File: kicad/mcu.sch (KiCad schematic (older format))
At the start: 25 parts, among them J7 UEXT, U2 STM32G431CBTx, U6 24AA01, Y1 8MHz

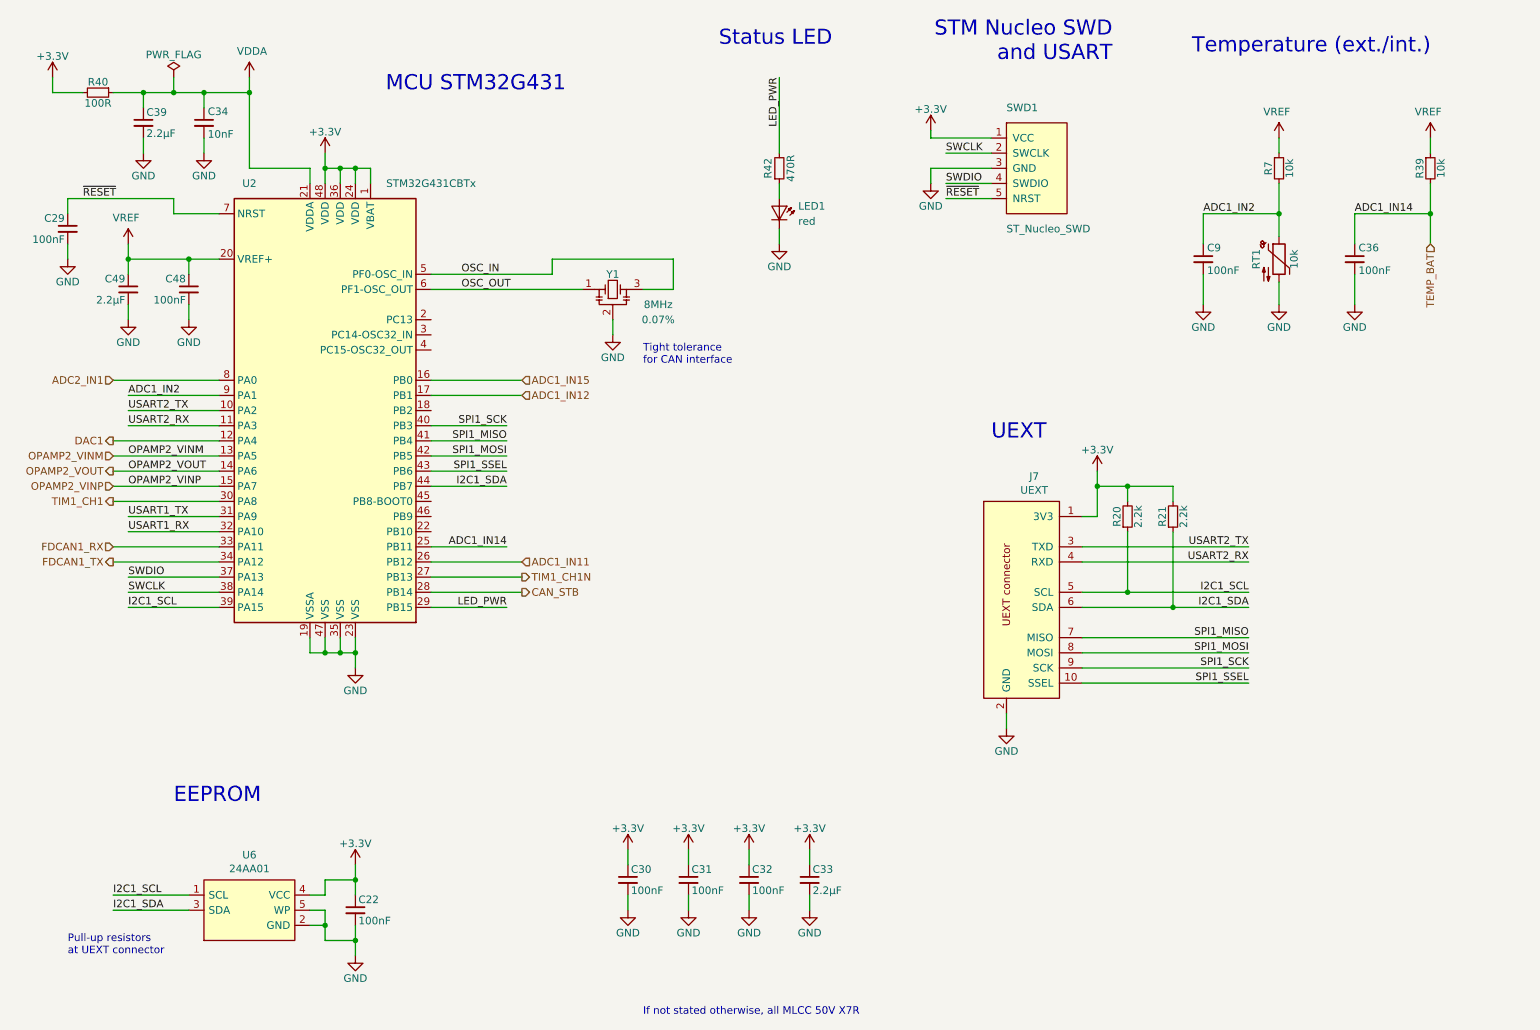
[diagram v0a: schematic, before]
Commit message: Fix errors after first prototype build-up
- Collision of capacitors with MOSFET clamps
- BOOT0 pin tied to GND
- Assignment of a few previously unasigned passives
- Add optional debug serial connector
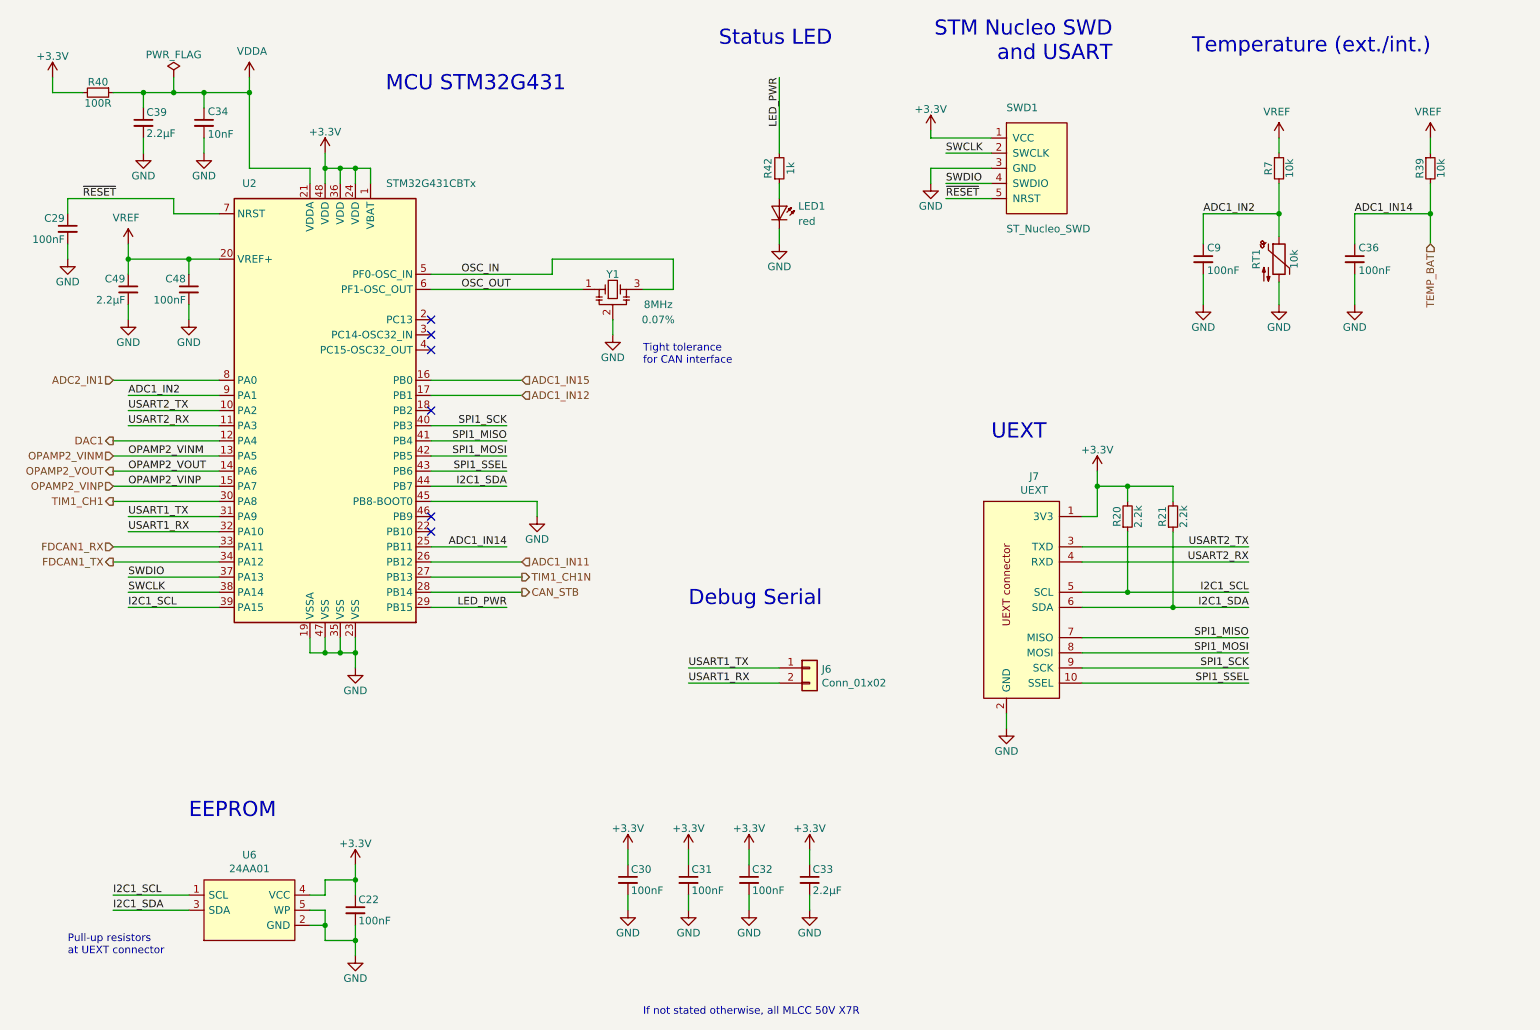
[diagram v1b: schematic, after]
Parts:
- added J6: Conn_01x02, Connector_PinHeader_2.54mm:PinHeader_1x02_P2.54mm_Vertical, symbol Connector_Generic:Conn_01x02
- R42: value 470R -> 1k; PartNumber RC0603FR-07470RL -> RC0603FR-071KL
- SWD1: Manufacturer (none) -> Any; PartNumber (none) -> Standard 2.54 mm pitch 1x5 pin header
- U2: Manufacturer (none) -> ST Microelectronics; PartNumber (none) -> STM32G431CBT6
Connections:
- net GND: now also U2.45 (PB8-BOOT0)
- net USART1_RX: now also J6.2 (Pin_2)
- net USART1_TX: now also J6.1 (Pin_1)
- no-connect marks 0 -> 6
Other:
- note added: "Debug Serial"
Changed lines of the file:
@@
 Sheet 4 5
 Title "MPPT 2420 RC"
-Date "2020-02-20"
-Rev "0.1"
+Date "2020-05-30"
+Rev "0.1.1"
 Comp "Libre Solar Technologies GmbH"
 Comment1 "Author: Martin Jäger"
@@
 P 6000 2000
 F 0 "R42" V 5925 2000 50  0000 C CNN
-F 1 "470R" V 6075 2000 50  0000 C CNN
+F 1 "1k" V 6075 2000 50  0000 C CNN
 F 2 "LibreSolar:R_0603_1608" H 6000 2000 50  0001 C CNN
 F 3 "" H 6000 2000 50  0000 C CNN
 F 4 "Yageo" H -3500 -2900 50  0001 C CNN "Manufacturer"
-F 5 "RC0603FR-07470RL" H -3500 -2900 50  0001 C CNN "PartNumber"
+F 5 "RC0603FR-071KL" H -3500 -2900 50  0001 C CNN "PartNumber"
 	1    6000 2000
 	1    0    0    1
@@
 F 2 "Connector_PinHeader_2.54mm:PinHeader_1x05_P2.54mm_Vertical" H 7700 1400 30  0001 C CIN
 F 3 "" H 7850 2050 60  0001 C CNN
+F 4 "Any" H 7700 2000 50  0001 C CNN "Manufacturer"
+F 5 "Standard 2.54 mm pitch 1x5 pin header" H 7700 2000 50  0001 C CNN "PartNumber"
 	1    7700 2000
 	1    0    0    -1
@@
 	1    0    0    -1
 $EndComp
-Text Notes 2000 6200 0    100  ~ 0
+Text Notes 2100 6300 0    100  ~ 0
 EEPROM
 $Comp
@@
 F 2 "Package_QFP:LQFP-48_7x7mm_P0.5mm" H 2550 2100 50  0001 R CNN
 F 3 "https://www.st.com/resource/en/datasheet/stm32g431cb.pdf" H 3000 3600 50  0001 C CNN
+F 4 "ST Microelectronics" H 3000 3600 50  0001 C CNN "Manufacturer"
+F 5 "STM32G431CBT6" H 3000 3600 50  0001 C CNN "PartNumber"
 	1    3000 3600
 	-1   0    0    -1
@@
 	1600 4100 2300 4100
 $Comp
-L LibreSolar:VREF #PWR?
+L LibreSolar:VREF #PWR0104
 U 1 1 5E68A8BB
 P 9300 1800
-F 0 "#PWR?" H 9300 1650 50  0001 C CNN
+F 0 "#PWR0104" H 9300 1650 50  0001 C CNN
 F 1 "VREF" H 9315 1973 50  0000 C CNN
 F 2 "" H 9300 1800 50  0001 C CNN
@@
 $EndComp
 $Comp
-L LibreSolar:VREF #PWR?
+L LibreSolar:VREF #PWR0107
 U 1 1 5E68C250
 P 10300 1800
-F 0 "#PWR?" H 10300 1650 50  0001 C CNN
+F 0 "#PWR0107" H 10300 1650 50  0001 C CNN
 F 1 "VREF" H 10315 1973 50  0000 C CNN
 F 2 "" H 10300 1800 50  0001 C CNN
@@
 	-1   0    0    -1
 $EndComp
+NoConn ~ 3700 4300
+NoConn ~ 3700 4400
+$Comp
+L power:GND #PWR0125
+U 1 1 5EC4B11B
+P 4400 4300
+F 0 "#PWR0125" H 4400 4050 50  0001 C CNN
+F 1 "GND" H 4400 4150 50  0000 C CNN
+F 2 "" H 4400 4300 50  0000 C CNN
+F 3 "" H 4400 4300 50  0000 C CNN
+	1    4400 4300
+	1    0    0    -1
+$EndComp
+Wire Wire Line
+	3700 4200 4400 4200
+Wire Wire Line
+	4400 4200 4400 4300
+NoConn ~ 3700 3000
+NoConn ~ 3700 3100
+NoConn ~ 3700 3200
+NoConn ~ 3700 3600
+$Comp
+L Connector_Generic:Conn_01x02 J6
+U 1 1 5ED70582
+P 6200 5300
+F 0 "J6" H 6280 5292 50  0000 L CNN
+F 1 "Conn_01x02" H 6280 5201 50  0000 L CNN
+F 2 "Connector_PinHeader_2.54mm:PinHeader_1x02_P2.54mm_Vertical" H 6200 5300 50  0001 C CNN
+F 3 "~" H 6200 5300 50  0001 C CNN
+	1    6200 5300
+	1    0    0    -1
+$EndComp
+Wire Wire Line
+	6000 5300 5400 5300
+Wire Wire Line
+	6000 5400 5400 5400
+Text Label 5400 5300 0    50   ~ 0
+USART1_TX
+Text Label 5400 5400 0    50   ~ 0
+USART1_RX
+Text Notes 5400 4900 0    100  ~ 0
+Debug Serial
 $EndSCHEMATC

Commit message: Fix some references and part numbers
See issues #3, #5, #7, #8 and #9.
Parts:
- C34: Manufacturer (none) -> Murata; PartNumber (none) -> GCM188R72A103KA37D; Remarks 50V, X7R -> 100V, X7R
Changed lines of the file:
@@
 F 2 "LibreSolar:C_0603_1608" H 2200 1700 50  0001 C CNN
 F 3 "" H 2200 1700 50  0000 C CNN
-F 4 "50V, X7R" H 2200 1700 50  0001 C CNN "Remarks"
+F 4 "100V, X7R" H 2200 1700 50  0001 C CNN "Remarks"
+F 5 "Murata" H 2200 1700 50  0001 C CNN "Manufacturer"
+F 6 "GCM188R72A103KA37D" H 2200 1700 50  0001 C CNN "PartNumber"
 	1    2200 1700
 	1    0    0    -1

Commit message: Clean up BOM and add build folder for generated files
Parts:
- LED1: symbol Project:D_LED -> LibreSolar:LED
- U6: value 24AA01 -> 24AA32; symbol LibreSolar:24AA01 -> LibreSolar:24AAxx-OT
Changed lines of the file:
@@
 $EndComp
 $Comp
-L Project:D_LED LED1
+L LibreSolar:LED LED1
 U 1 1 58AE0EA3
 P 6000 2300
@@
 Tight tolerance\nfor CAN interface
 $Comp
-L LibreSolar:24AA01 U6
+L LibreSolar:24AAxx-OT U6
 U 1 1 5929D79A
 P 2500 6900
+AR Path="/5929D79A" Ref="U6"  Part="1"
+AR Path="/58A68DCB/5929D79A" Ref="U6"  Part="1"
 F 0 "U6" H 2500 7265 50  0000 C CNN
-F 1 "24AA01" H 2500 7174 50  0000 C CNN
+F 1 "24AA32" H 2500 7174 50  0000 C CNN
 F 2 "LibreSolar:SOT-23-5" H 2500 6500 50  0001 C CNN
 F 3 "" H 2500 7150 60  0000 C CNN
